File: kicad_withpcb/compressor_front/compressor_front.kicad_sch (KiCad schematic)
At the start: 33 parts, among them J1 MAIN BOARD, SW1 BYPASS, SW2 INT/EXT, SW3 HPF DEFEAT, SW4 LINK, U10 LM3915, U9 LM3914

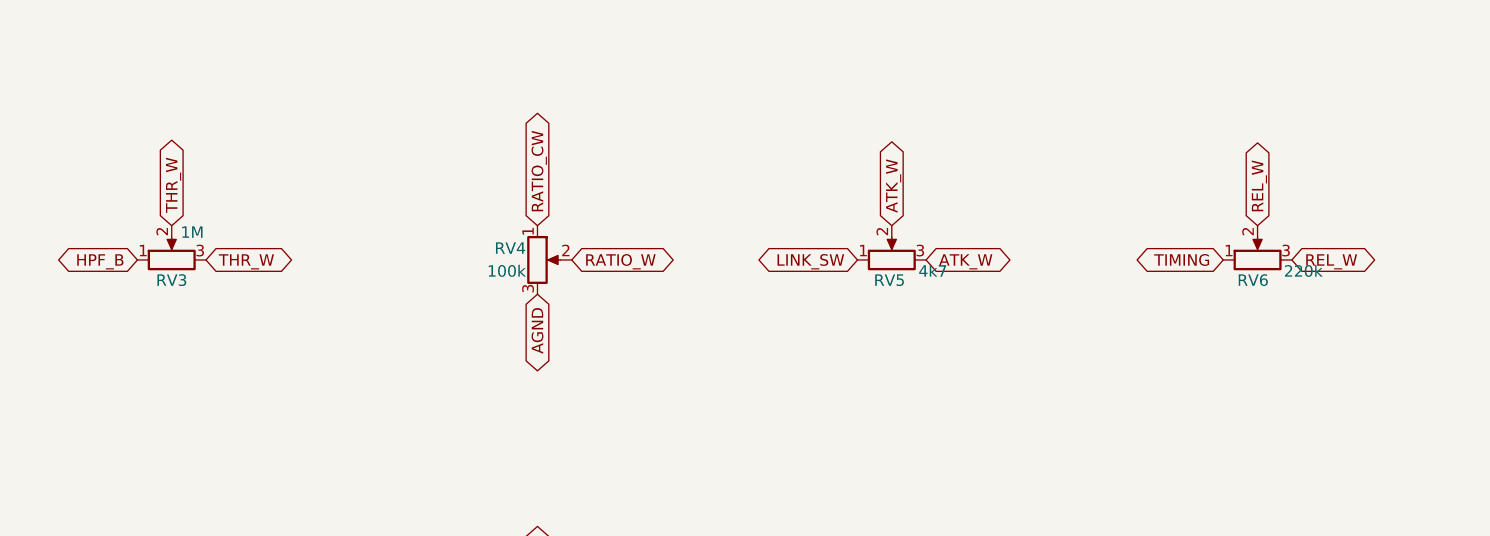
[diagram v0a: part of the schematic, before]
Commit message: Carry the new values onto both boards' schematics and layouts
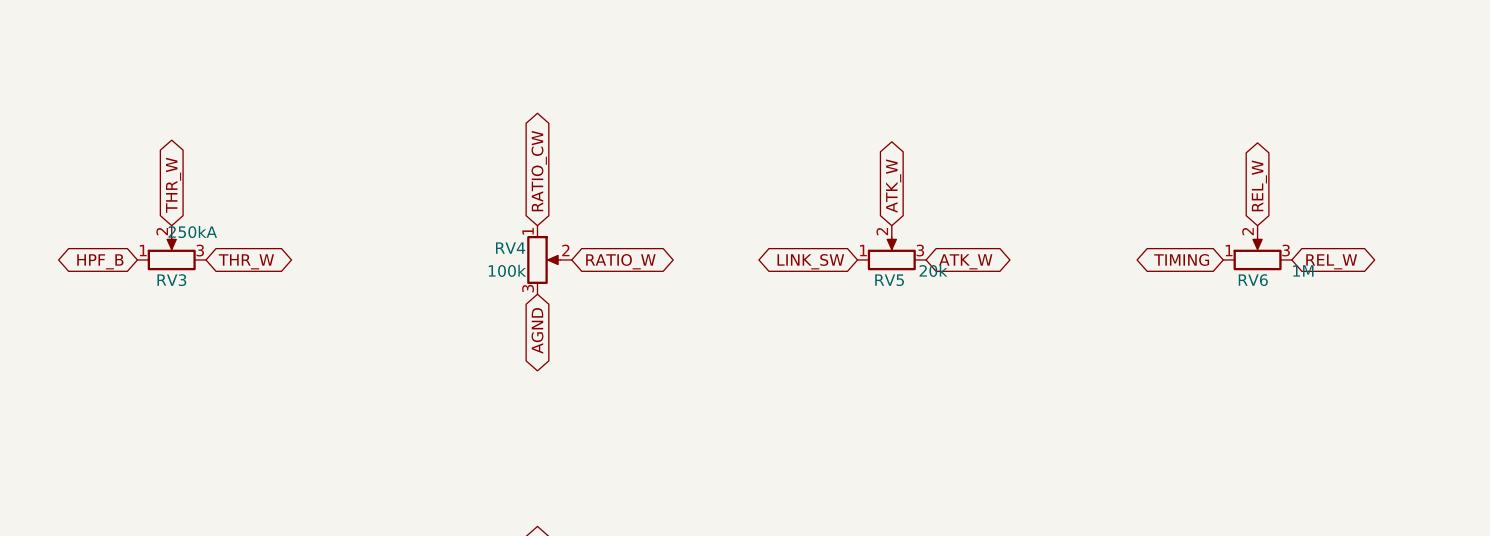
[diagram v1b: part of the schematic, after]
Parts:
- RV3: value 1M -> 250kA
- RV5: value 4k7 -> 20k
- RV6: value 220k -> 1M
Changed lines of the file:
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@@
 			)
 		)
-		(property "Value" "220k"
+		(property "Value" "1M"
 			(at 275.59 50.8 90)
 			(show_name no)
@@
 			)
 		)
-		(property "Value" "4k7"
+		(property "Value" "20k"
 			(at 234.442 50.8 90)
 			(show_name no)
@@
 			)
 		)
-		(property "Value" "1M"
+		(property "Value" "250kA"
 			(at 152.146 46.482 90)
 			(show_name no)

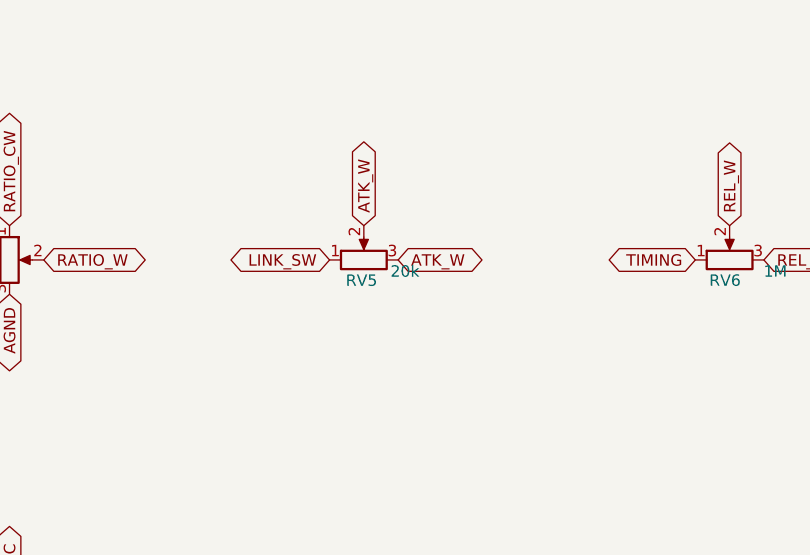
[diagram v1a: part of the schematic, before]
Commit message: Retune attack and release: R45 220R, R46 47R, RV5 10k, R47 15k
The first pass ran the attack too slow (9 to 103 ms against a 2.7 to
50 ms target). Results are regenerated in the next commit.
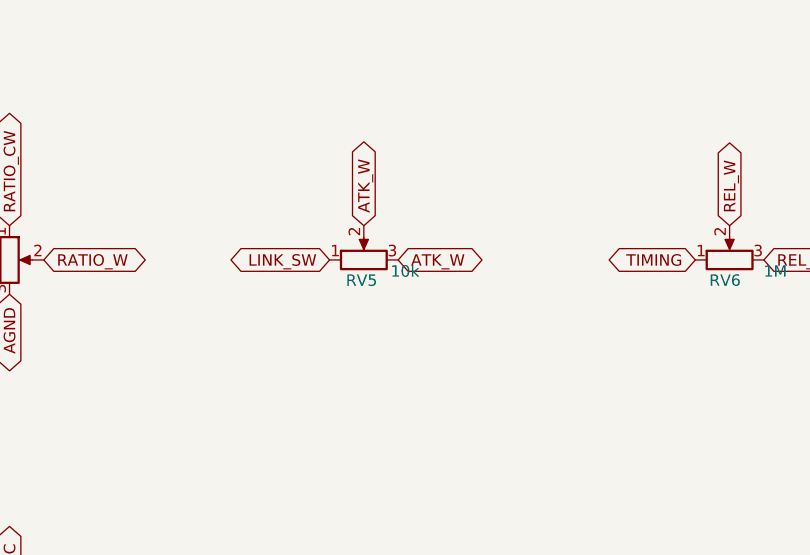
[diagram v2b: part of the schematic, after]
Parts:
- RV5: value 20k -> 10k
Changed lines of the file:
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@@
 			)
 		)
-		(property "Value" "20k"
+		(property "Value" "10k"
 			(at 234.442 50.8 90)
 			(show_name no)

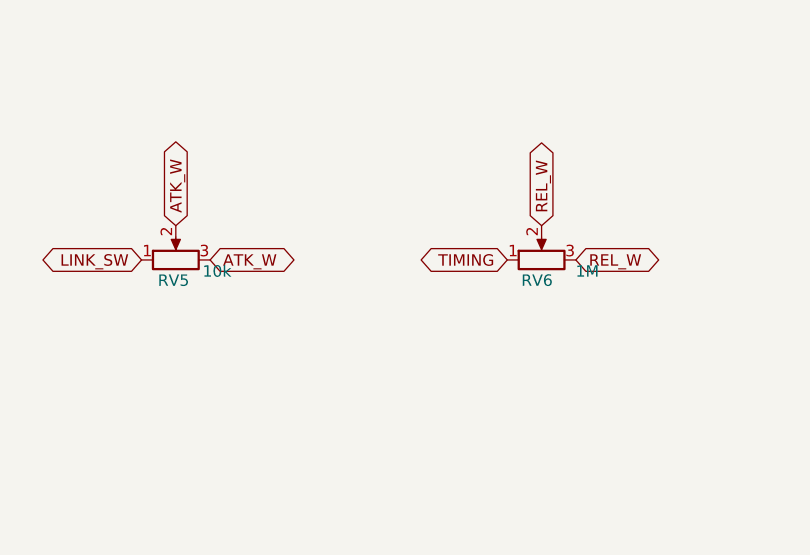
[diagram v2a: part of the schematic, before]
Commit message: Stop the fast-attack overshoot: C22 47u to 4u7
C22 made STA lag STB by about 60 ms, so when CTRL-B pulled the
reference node down the steering kept moving after the control
voltage had settled, overshooting by up to 20 dB. With 4u7 the two
sides track and the overshoot is about 1 dB. RV5 back to 4k7 and RV6
to 500k, since the attack and release run slower without it.
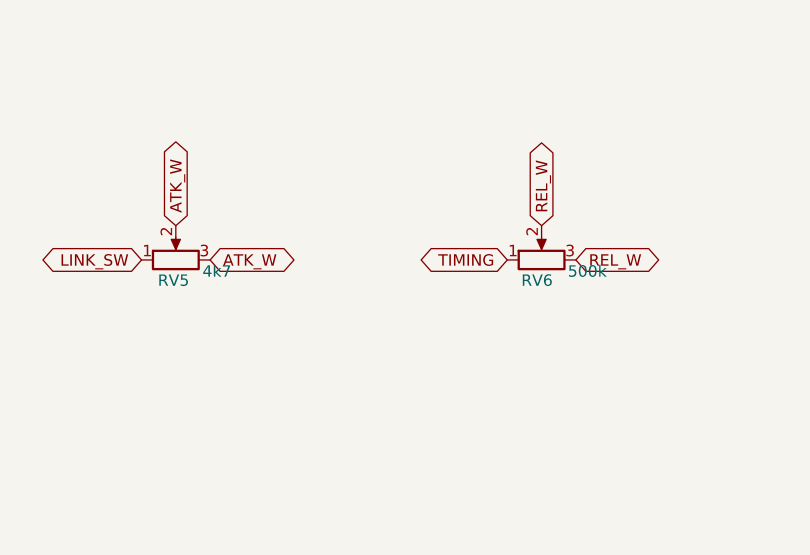
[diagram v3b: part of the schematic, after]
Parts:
- RV5: value 10k -> 4k7
- RV6: value 1M -> 500k
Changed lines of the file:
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@@
 			)
 		)
-		(property "Value" "1M"
+		(property "Value" "500k"
 			(at 275.59 50.8 90)
 			(show_name no)
@@
 			)
 		)
-		(property "Value" "10k"
+		(property "Value" "4k7"
 			(at 234.442 50.8 90)
 			(show_name no)

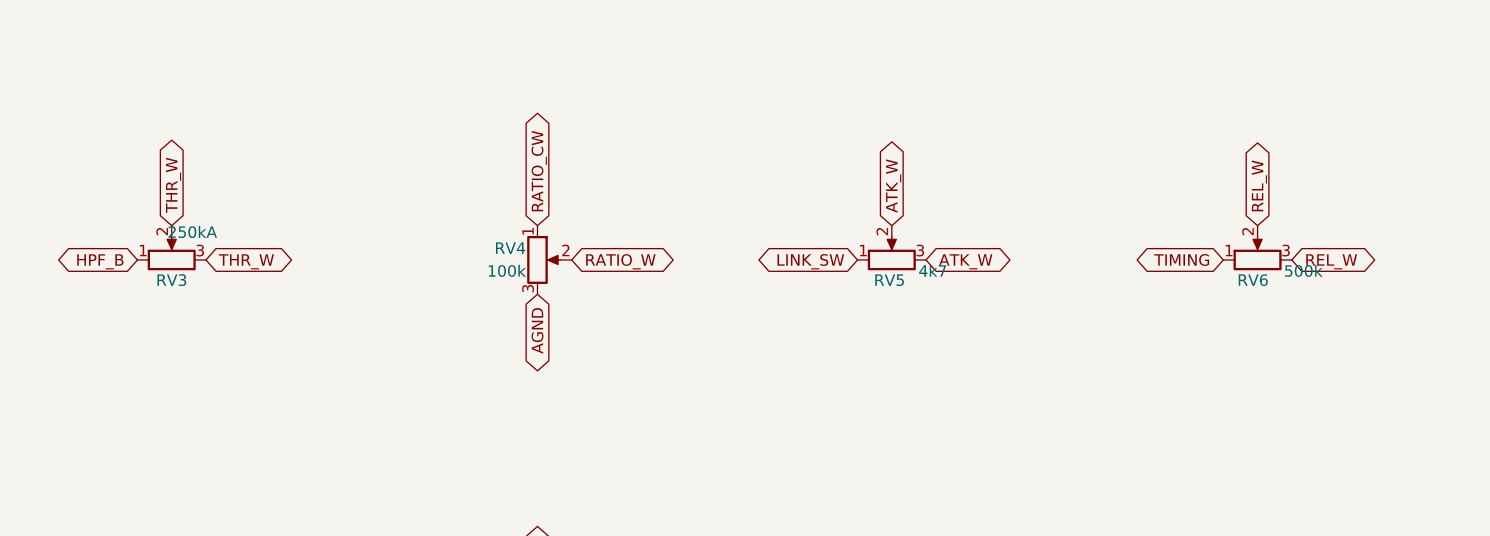
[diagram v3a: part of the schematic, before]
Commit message: Use 100k pots for RV3 and RV6, and steady the sidechain high-pass
RK09K pots stop at 100k. RV3 becomes 100kA with R35 1k and R36 82k,
which scales the threshold network and keeps the -20 to +20 dBu range.
RV6 becomes 100k, so the slowest release drops to about 0.4 s.

R35 at 2k4 had also loaded the sidechain high-pass (C14 into R38), so at
the lowest threshold its corner rose to about 400 Hz. R38 1k and C14 2u2
hold it between about 80 and 160 Hz across the threshold knob.
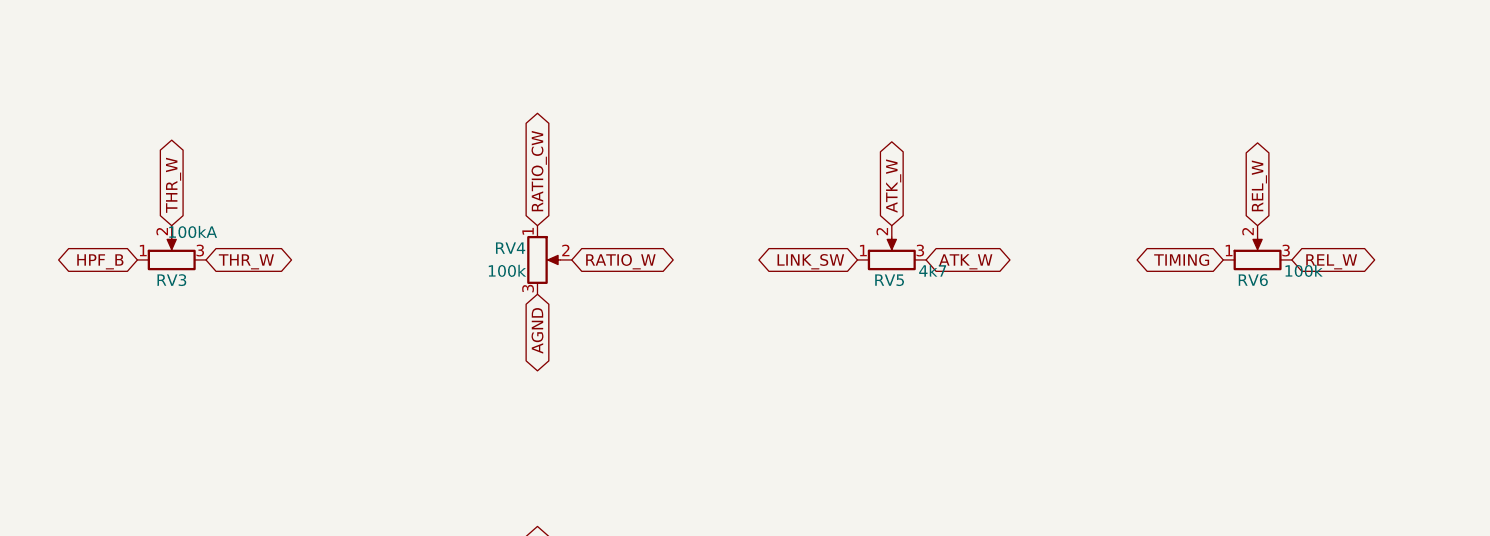
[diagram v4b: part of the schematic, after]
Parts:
- RV3: value 250kA -> 100kA
- RV6: value 500k -> 100k
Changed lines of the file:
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@@
 			)
 		)
-		(property "Value" "500k"
+		(property "Value" "100k"
 			(at 275.59 50.8 90)
 			(show_name no)
@@
 			)
 		)
-		(property "Value" "250kA"
+		(property "Value" "100kA"
 			(at 152.146 46.482 90)
 			(show_name no)

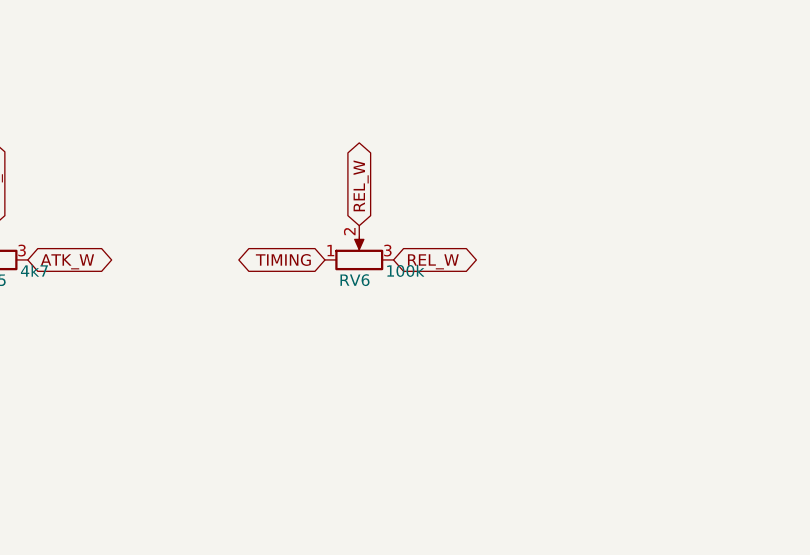
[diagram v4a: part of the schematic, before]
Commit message: Put RV6 back to 500k, to be a Bourns PTV09
RK09K stops at 100k, which would cut the slowest release to about 0.4 s.
Lyn chose a 500k Bourns PTV09 instead, keeping it near 1.8 s.
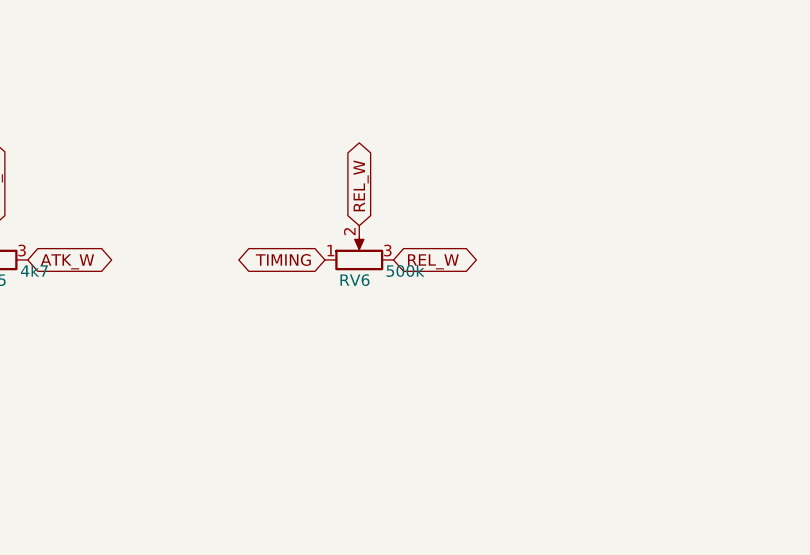
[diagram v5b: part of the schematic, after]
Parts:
- RV6: value 100k -> 500k
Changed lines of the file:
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@@
 			)
 		)
-		(property "Value" "100k"
+		(property "Value" "500k"
 			(at 275.59 50.8 90)
 			(show_name no)

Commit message: Swap the front panel toggles for Altronics' Salecom mini toggles
BYPASS is now an S1350 (DPDT) and KEY, HPF and LINK are S1315 (SPDT);
the S1332 centre-off shares the SPDT footprint. Footprints and STEP
models follow the drawings on the Altronics product pages: pins on
4.70 mm with 1.3 mm holes, DPDT rows 4.83 mm apart, bodies 6.9 or 11.4
by 12.7 mm standing 10.4 mm off the board, 1/4-40 bushing 8.9 mm long.

The toggles move 0.25 mm inboard (x 7.15 / 30.95) so the S1350 body
stays on the 35 mm board, and the pot courtyard is trimmed to its pads
so it doesn't overlap the S1350. C38 moves 1 mm up, clear of the SW2
body. The switch nets and the nets crowding J1 were re-routed with
Freerouting: DRC 0 errors, 0 unconnected, schematic parity clean.

The panel's toggle holes go from 5.2 to 6.5 mm, and make_panel.py now
checks the switch and pot bodies behind the panel against each other
and the front board. The board now sits about 10.6 mm behind the panel,
set by the 9 mm pots; the toggles' long bushing no longer needs a
thinned panel, but the pots' 5 mm one does.
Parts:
- SW1: footprint compressor_front:SW_Toggle_SubMini_DPDT_Jaycar_ST0310 -> compressor_front:SW_Toggle_Mini_DPDT_Salecom_S1350
- SW2, SW3, SW4: footprint compressor_front:SW_Toggle_SubMini_SPDT_Jaycar_ST0300 -> compressor_front:SW_Toggle_Mini_SPDT_Salecom_S1315
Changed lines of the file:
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@@
 			)
 		)
-		(property "Footprint" "compressor_front:SW_Toggle_SubMini_SPDT_Jaycar_ST0300"
+		(property "Footprint" "compressor_front:SW_Toggle_Mini_SPDT_Salecom_S1315"
 			(at 277.622 104.14 0)
 			(hide yes)
@@
 			)
 		)
-		(property "Footprint" "compressor_front:SW_Toggle_SubMini_SPDT_Jaycar_ST0300"
+		(property "Footprint" "compressor_front:SW_Toggle_Mini_SPDT_Salecom_S1315"
 			(at 229.87 95.25 0)
 			(hide yes)
@@
 			)
 		)
-		(property "Footprint" "compressor_front:SW_Toggle_SubMini_SPDT_Jaycar_ST0300"
+		(property "Footprint" "compressor_front:SW_Toggle_Mini_SPDT_Salecom_S1315"
 			(at 190.5 95.25 0)
 			(hide yes)
@@
 			)
 		)
-		(property "Footprint" "compressor_front:SW_Toggle_SubMini_DPDT_Jaycar_ST0310"
+		(property "Footprint" "compressor_front:SW_Toggle_Mini_DPDT_Salecom_S1350"
 			(at 110.49 95.25 0)
 			(hide yes)
@@
 			)
 		)
-		(property "Footprint" "compressor_front:SW_Toggle_SubMini_DPDT_Jaycar_ST0310"
+		(property "Footprint" "compressor_front:SW_Toggle_Mini_DPDT_Salecom_S1350"
 			(at 149.86 95.25 0)
 			(hide yes)
